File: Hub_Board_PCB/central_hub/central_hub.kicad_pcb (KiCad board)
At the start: 2 copper layers, 0.6 x 1.7 mm, 111 parts, among them J1 CAN_OUT, J2 Conn_01x02, J3 Screw_Terminal_01x08, J4 Screw_Terminal_01x08, J5 CSP-USC16-TR, J6 Screw_Terminal_01x04, J7 Conn_01x03, J8 Conn_01x02, J9 Screw_Terminal_01x04, Q1 BSS138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

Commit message: Central hub layout first draft (+ some changes to motor driver)
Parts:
- removed SW1: SW_Push, Button_Switch_SMD:SW_Push_1P1T_NO_6x6mm_H9.5mm
- removed TP1, TP6: TestPoint, TestPoint:TestPoint_Pad_D1.0mm
- added C20: 10nF, Capacitor_SMD:C_0603_1608Metric, B.Cu at (75.8, 7.70)
- added C21: 10nF, Capacitor_SMD:C_0603_1608Metric, B.Cu at (73.6, 6.40)
- added C22: 10nF, Capacitor_SMD:C_0603_1608Metric, B.Cu at (71.4, 5.00)
- added H1: MountingHole, MountingHole:MountingHole_3mm, F.Cu at (3.00, 3.00)
- added H2: MountingHole, MountingHole:MountingHole_3mm, F.Cu at (105.0, 3.00)
- added H3: MountingHole, MountingHole:MountingHole_3mm, F.Cu at (3.00, 58.7)
- added H4: MountingHole, MountingHole:MountingHole_3mm, F.Cu at (105.0, 58.7)
- C7, C9: moved to B.Cu
- moved J1 283.5 mm to (2.70, 50.3)
- moved R19 269.4 mm to (16.4, 33.6), turned to 0 degrees
- moved R18 265.8 mm to (6.35, 49.0), turned to -90 degrees
- moved D6 264.8 mm to (20.6, 33.6), turned to 180 degrees
- moved R20 263.2 mm to (16.4, 36.7), turned to 0 degrees
- moved D5 262.5 mm to (9.53, 49.0), turned to -90 degrees
- moved D7 258.7 mm to (20.6, 36.7), turned to 180 degrees
- moved U4 248.3 mm to (16.7, 49.0), turned to 90 degrees
- moved Y2 246.9 mm to (37.6, 58.3)
- moved C11 245.8 mm to (33.5, 54.5), turned to 180 degrees
- moved C13 242.7 mm to (36.9, 54.5), turned to 0 degrees
- moved C14 239.3 mm to (21.2, 49.1)
- moved C12 236.9 mm to (27.7, 44.2), turned to 90 degrees
- moved U3 236.9 mm to (33.3, 47.9)
- moved TP9 223.5 mm to (28.7, 40.3)
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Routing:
- net +5V: track 0.00 -> 297.1 mm, vias 0 -> 20
- net +3.3V: track 0.00 -> 169.5 mm, vias 0 -> 11
- net D10: track 0.00 -> 95.9 mm, vias 0 -> 2
- net D13: track 0.00 -> 90.2 mm, vias 0 -> 2
- net D11: track 0.00 -> 80.7 mm, vias 0 -> 2
- net D12: track 0.00 -> 63.1 mm, vias 0 -> 2
- net D5: track 0.00 -> 56.8 mm, vias 0 -> 2
- net GND: track 0.00 -> 56.0 mm, vias 0 -> 48
- net D1: track 0.00 -> 55.7 mm, vias 0 -> 2
- net D0: track 0.00 -> 53.6 mm, vias 0 -> 2
- net D4: track 0.00 -> 51.0 mm, vias 0 -> 2
- net D7: track 0.00 -> 48.5 mm
- net D6: track 0.00 -> 48.4 mm, vias 0 -> 1
- net D2: track 0.00 -> 47.0 mm, vias 0 -> 1
- net D3: track 0.00 -> 45.3 mm, vias 0 -> 1
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- added copper zone on B.Cu, net +12V
- added copper zone on F.Cu, net +12V
- added copper zone on F.Cu, net +5V
- added copper zone on F.Cu, net -BATT
- added copper zone on B.Cu, net GND
- added copper zone on F.Cu, net GND
- added copper zone on F.Cu, net Net-(C25-Pad2)
- added copper zone on F.Cu, net Net-(C27-Pad2)
- added copper zone on F.Cu, net Net-(C30-Pad2)
- added copper zone on F.Cu, net Net-(U7-BST)
- added copper zone on F.Cu, net Net-(U7-SW)
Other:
- board size 0.6 x 1.7 mm -> 108 x 61.7 mm

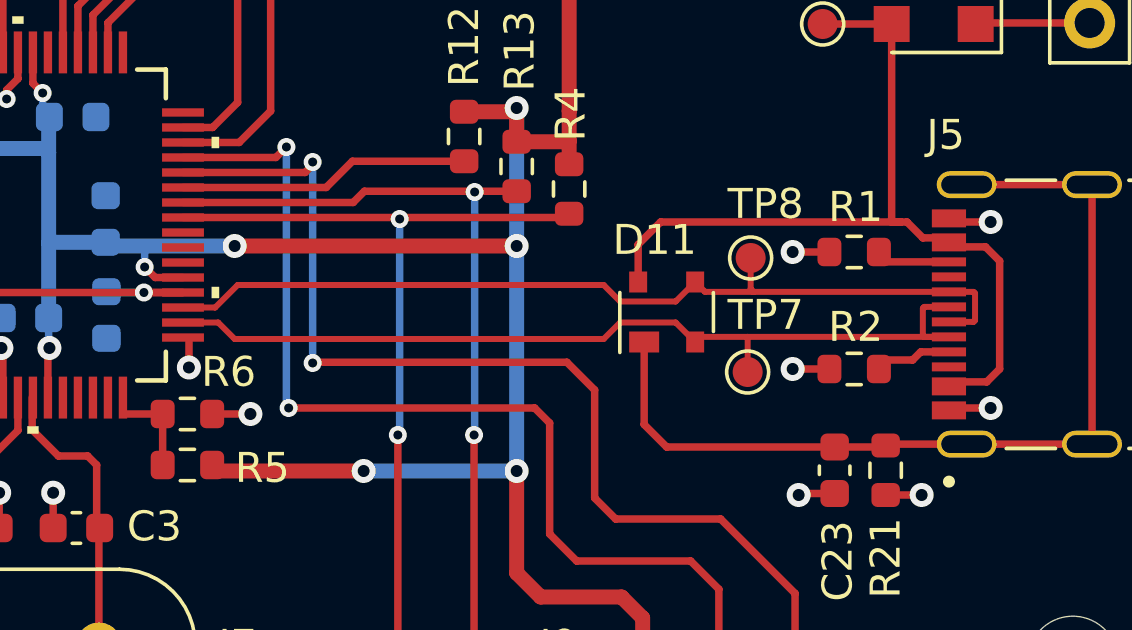
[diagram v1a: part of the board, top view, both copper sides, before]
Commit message: Small changes to USB connector d+ and d- traces
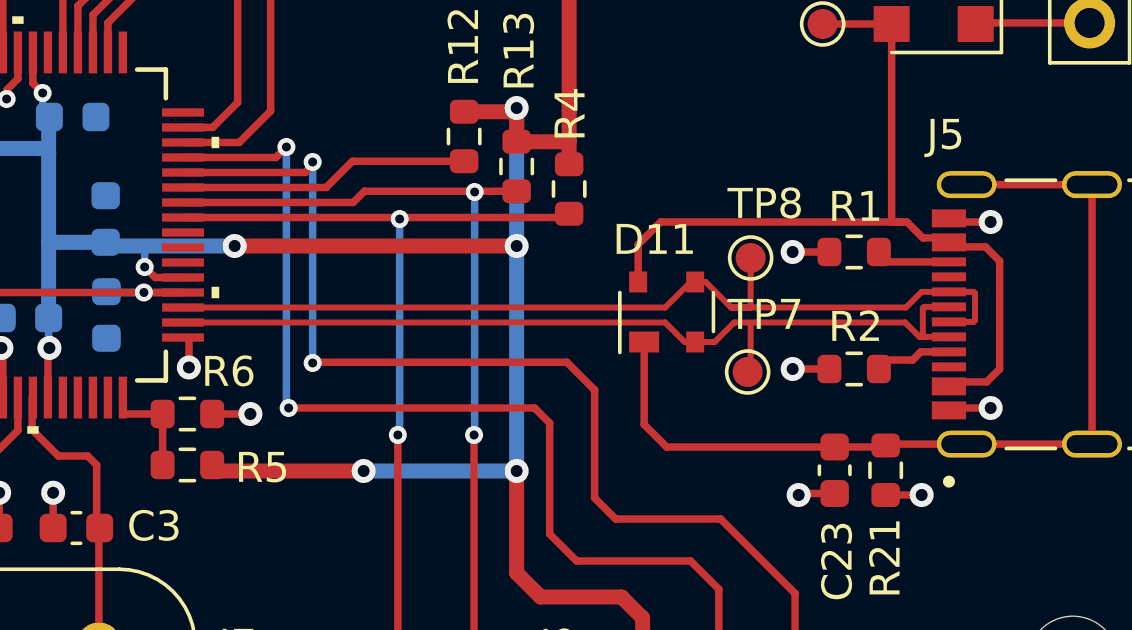
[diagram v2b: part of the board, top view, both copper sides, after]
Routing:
- net USB_D+: track 30.3 -> 31.4 mm
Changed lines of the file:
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@@
   (segment (start 100.04 44.62925) (end 100.91 44.62925) (width 0.25) (layer "F.Cu") (net 25))
   (segment (start 99.51075 44.1) (end 100.04 44.62925) (width 0.25) (layer "F.Cu") (net 25))
-  (segment (start 92.45 48.1) (end 91.8 47.45) (width 0.2) (layer "F.Cu") (net 26))
+  (segment (start 99.45 47.45) (end 99.92925 47.92925) (width 0.2) (layer "F.Cu") (net 26))
   (segment (start 100.09 47.92925) (end 100.91 47.92925) (width 0.2) (layer "F.Cu") (net 26))
-  (segment (start 91.8 47.45) (end 89.95 47.45) (width 0.2) (layer "F.Cu") (net 26))
+  (segment (start 89.95 47.45) (end 89.949181 47.450819) (width 0.2) (layer "F.Cu") (net 26))
+  (segment (start 92.1 48.1) (end 91.45 47.45) (width 0.2) (layer "F.Cu") (net 26))
   (segment (start 100.91 46.92925) (end 100.09 46.92925) (width 0.2) (layer "F.Cu") (net 26))
-  (segment (start 89.4 48) (end 77.1 48) (width 0.2) (layer "F.Cu") (net 26))
-  (segment (start 89.95 47.45) (end 89.4 48) (width 0.2) (layer "F.Cu") (net 26))
-  (segment (start 92.45 48.1) (end 92.62075 47.92925) (width 0.2) (layer "F.Cu") (net 26))
+  (segment (start 99.92925 47.92925) (end 100.09 47.92925) (width 0.2) (layer "F.Cu") (net 26))
+  (segment (start 92.45 48.1) (end 92.1 48.1) (width 0.2) (layer "F.Cu") (net 26))
+  (segment (start 91.45 47.45) (end 89.95 47.45) (width 0.2) (layer "F.Cu") (net 26))
+  (segment (start 93.75 47.45) (end 99.45 47.45) (width 0.2) (layer "F.Cu") (net 26))
   (segment (start 100.04 46.97925) (end 100.04 47.87925) (width 0.2) (layer "F.Cu") (net 26))
-  (segment (start 92.62075 47.92925) (end 94.2 47.92925) (width 0.2) (layer "F.Cu") (net 26))
+  (segment (start 92.45 48.1) (end 93.1 48.1) (width 0.2) (layer "F.Cu") (net 26))
   (segment (start 100.09 46.92925) (end 100.04 46.97925) (width 0.2) (layer "F.Cu") (net 26))
-  (segment (start 77.1 48) (end 76.550819 47.450819) (width 0.2) (layer "F.Cu") (net 26))
-  (segment (start 94.2 47.92925) (end 100.91 47.92925) (width 0.2) (layer "F.Cu") (net 26))
-  (segment (start 94.2 49.1) (end 94.2 47.92925) (width 0.2) (layer "F.Cu") (net 26))
+  (segment (start 93.1 48.1) (end 93.75 47.45) (width 0.2) (layer "F.Cu") (net 26))
   (segment (start 100.04 47.87925) (end 100.09 47.92925) (width 0.2) (layer "F.Cu") (net 26))
-  (segment (start 76.550819 47.450819) (end 75.3781 47.450819) (width 0.2) (layer "F.Cu") (net 26))
+  (segment (start 94.2 49.1) (end 94.3 49) (width 0.2) (layer "F.Cu") (net 26))
+  (segment (start 89.949181 47.450819) (end 75.3781 47.450819) (width 0.2) (layer "F.Cu") (net 26))
+  (segment (start 94.3 49) (end 94.3 47.5) (width 0.2) (layer "F.Cu") (net 26))
   (segment (start 101.73 47.42925) (end 100.91 47.42925) (width 0.2) (layer "F.Cu") (net 27))
-  (segment (start 92.45 46.1) (end 92.77925 46.42925) (width 0.2) (layer "F.Cu") (net 27))
+  (segment (start 99.476782 46.95) (end 99.997532 46.42925) (width 0.2) (layer "F.Cu") (net 27))
+  (segment (start 91.449307 46.950693) (end 75.3781 46.950693) (width 0.2) (layer "F.Cu") (net 27))
+  (segment (start 92.3 46.1) (end 91.449307 46.950693) (width 0.2) (layer "F.Cu") (net 27))
   (segment (start 101.73 46.42925) (end 101.78 46.47925) (width 0.2) (layer "F.Cu") (net 27))
   (segment (start 101.78 47.37925) (end 101.73 47.42925) (width 0.2) (layer "F.Cu") (net 27))
-  (segment (start 91.8 46.75) (end 89.95 46.75) (width 0.2) (layer "F.Cu") (net 27))
-  (segment (start 92.45 46.1) (end 91.8 46.75) (width 0.2) (layer "F.Cu") (net 27))
-  (segment (start 94.3 45.3) (end 94.3 46.32925) (width 0.2) (layer "F.Cu") (net 27))
-  (segment (start 92.77925 46.42925) (end 94.4 46.42925) (width 0.2) (layer "F.Cu") (net 27))
-  (segment (start 76.449307 46.950693) (end 75.3781 46.950693) (width 0.2) (layer "F.Cu") (net 27))
-  (segment (start 94.4 46.42925) (end 100.91 46.42925) (width 0.2) (layer "F.Cu") (net 27))
-  (segment (start 89.4 46.2) (end 77.2 46.2) (width 0.2) (layer "F.Cu") (net 27))
-  (segment (start 94.3 46.32925) (end 94.4 46.42925) (width 0.2) (layer "F.Cu") (net 27))
+  (segment (start 93.65 46.95) (end 99.476782 46.95) (width 0.2) (layer "F.Cu") (net 27))
+  (segment (start 92.45 46.1) (end 92.8 46.1) (width 0.2) (layer "F.Cu") (net 27))
+  (segment (start 93.65 46.95) (end 94.3 46.95) (width 0.2) (layer "F.Cu") (net 27))
+  (segment (start 94.3 46.95) (end 94.3 45.3) (width 0.2) (layer "F.Cu") (net 27))
+  (segment (start 92.8 46.1) (end 93.65 46.95) (width 0.2) (layer "F.Cu") (net 27))
+  (segment (start 99.997532 46.42925) (end 100.91 46.42925) (width 0.2) (layer "F.Cu") (net 27))
   (segment (start 100.91 46.42925) (end 101.73 46.42925) (width 0.2) (layer "F.Cu") (net 27))
-  (segment (start 77.2 46.2) (end 76.449307 46.950693) (width 0.2) (layer "F.Cu") (net 27))
   (segment (start 101.78 46.47925) (end 101.78 47.37925) (width 0.2) (layer "F.Cu") (net 27))
-  (segment (start 89.95 46.75) (end 89.4 46.2) (width 0.2) (layer "F.Cu") (net 27))
+  (segment (start 92.45 46.1) (end 92.3 46.1) (width 0.2) (layer "F.Cu") (net 27))
   (segment (start 3.166833 19.18) (end 2.85 18.863167) (width 0.25) (layer "F.Cu") (net 28))
   (segment (start 3.046833 18.88548) (end 3.046833 15.997313) (width 1) (layer "F.Cu") (net 28))

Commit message: Meeting layout updates
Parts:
- added R35: 0, Resistor_SMD:R_0402_1005Metric, F.Cu at (132.8, 75.6)
- added R36: 0, Resistor_SMD:R_0402_1005Metric, F.Cu at (130.7, 75.6)
- added R37: 0, Resistor_SMD:R_0402_1005Metric, F.Cu at (129.7, 75.6)
- added R7: 0, Resistor_SMD:R_0402_1005Metric, F.Cu at (99.6, 78.7)
- moved G*** 110.6 mm to (80.0, 97.1)
- moved R19 83.0 mm to (89.5, 72.9), turned to -90 degrees
- moved D6 81.5 mm to (89.5, 77.1), turned to 90 degrees
- moved R20 78.8 mm to (86.4, 72.9), turned to -90 degrees
- moved TP9 78.4 mm to (96.7, 79.2)
- moved D7 77.2 mm to (86.4, 77.1), turned to 90 degrees
- moved C11 76.4 mm to (100.8, 90.8)
- moved C13 76.4 mm to (104.2, 90.8)
- moved U3 76.4 mm to (100.5, 84.2)
- moved C12 76.4 mm to (95.0, 80.5)
- moved C14 76.4 mm to (88.5, 85.4)
- moved U4 76.4 mm to (84.0, 85.3)
- moved Y2 76.4 mm to (104.9, 94.6)
- moved TP4 75.3 mm to (107.2, 60.1)
- moved TP5 72.6 mm to (100.0, 61.8)
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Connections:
- U1 pad 34: D11 -> Net-(U1-CTX0/TDO/SWO/GTIOC1A/P109)
- U1 pad 36: D13 -> Net-(U1-GTIOC3A/P111)
- U1 pad 37: D10 -> Net-(U1-GTIOC3B/P112)
- U3 pad 17: D12 -> Net-(U3-SO)
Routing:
- net /MCU/P012: track 18.7 -> 43.9 mm, vias 0 -> 2
- net /MCU/P013: track 19.3 -> 41.5 mm, vias 0 -> 2
- net D11: track 80.7 -> 63.0 mm
- net D10: track 95.9 -> 78.3 mm
- net D12: track 63.1 -> 46.3 mm
- net +5V: track 297.1 -> 284.7 mm
- net +3.3V: track 169.5 -> 157.5 mm
- net D7: track 48.5 -> 38.8 mm
- net D6: track 48.4 -> 39.1 mm
- net D0: track 53.6 -> 44.4 mm
- net D1: track 55.7 -> 46.5 mm
- net /CAN/CAN_HI: track 13.2 -> 22.0 mm
- net /CAN/CAN_LOW: track 13.3 -> 22.0 mm
- net Net-(D6-K): track 30.5 -> 21.9 mm
- net D2: track 47.0 -> 38.5 mm
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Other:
- board text added: "FYDP 2024 Group 26 - Ethan Gilbert - Brandon Phu - Jonathon Ko - Ben Flack"

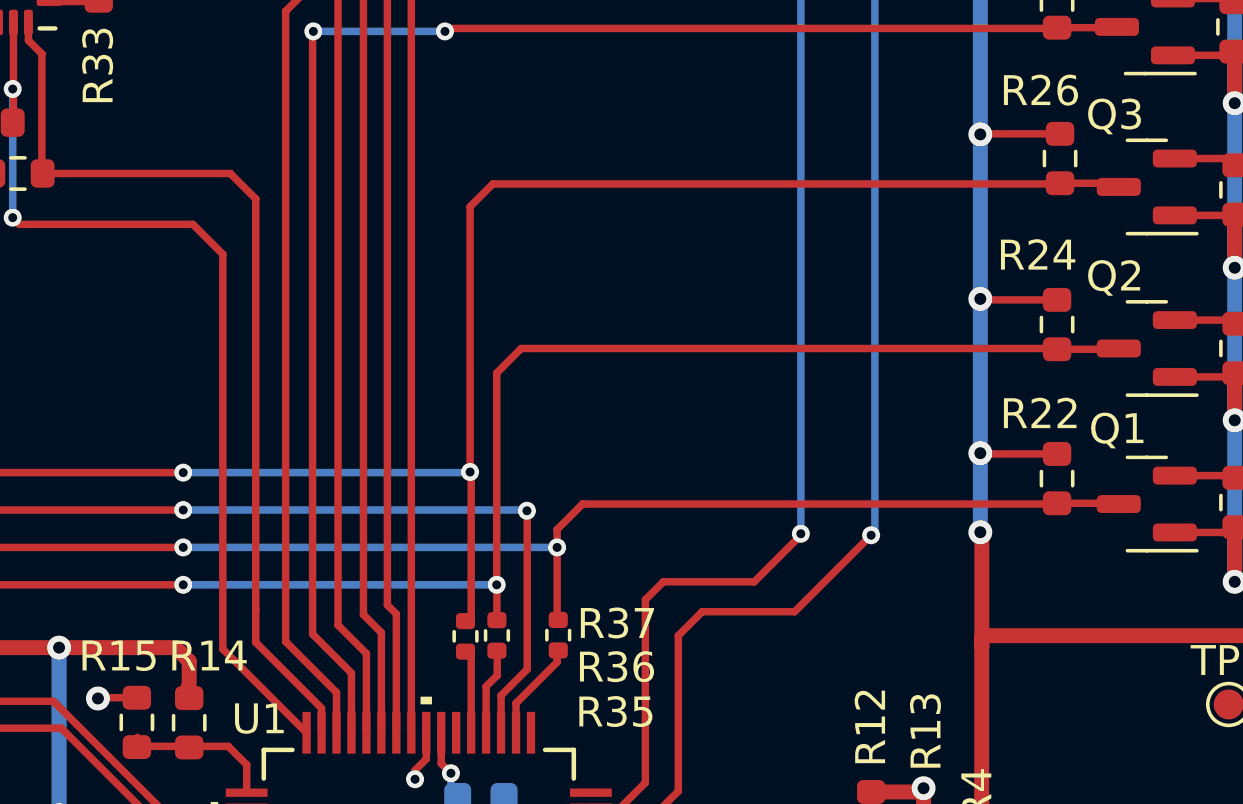
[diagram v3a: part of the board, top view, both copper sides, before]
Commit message: added additional cs pin for display/can
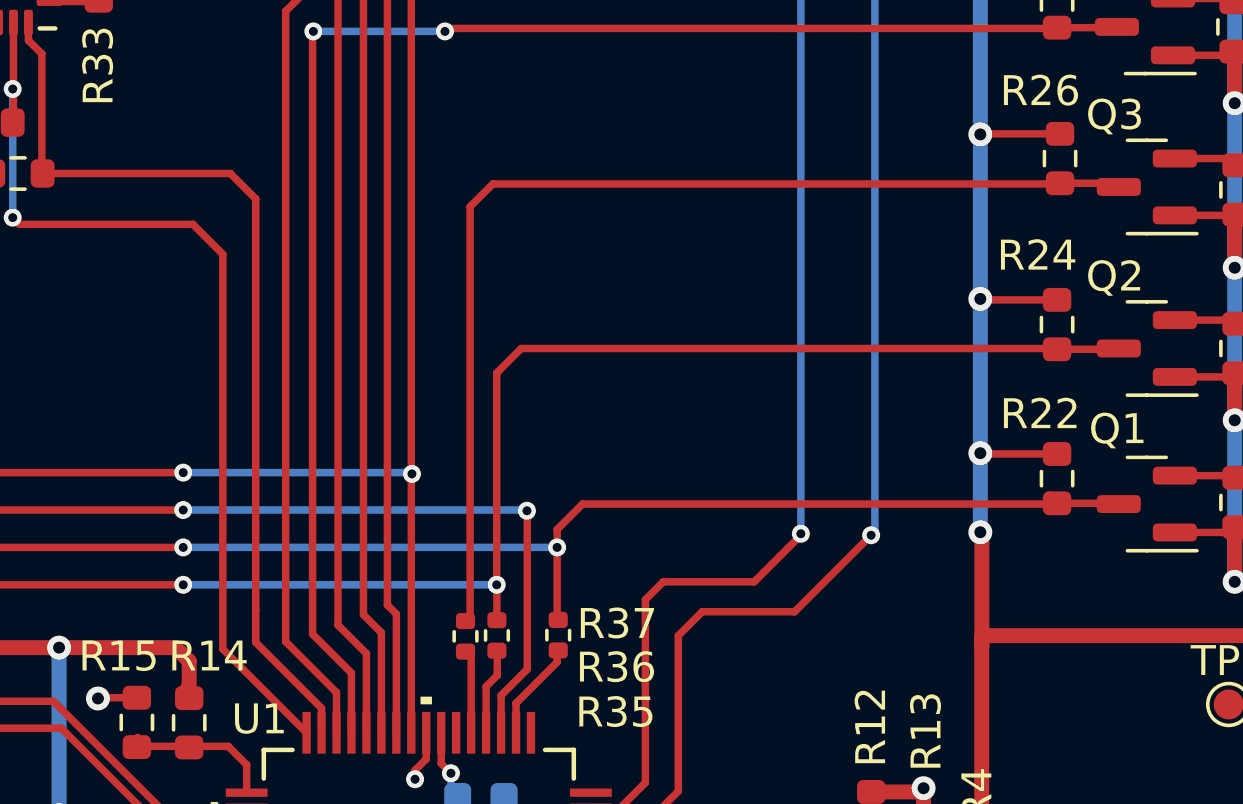
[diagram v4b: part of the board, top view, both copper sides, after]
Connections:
- U3 pad 18: D10 -> D7
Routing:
- net D10: track 78.3 -> 36.0 mm, vias 2 -> 0
- net D7: track 38.8 -> 79.0 mm, vias 0 -> 2
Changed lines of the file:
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@@
       (net 124 "Net-(U3-SO)") (pinfunction "SO") (pintype "output"))
     (pad "18" smd roundrect (at 2.8625 -1.625 90) (size 1.475 0.4) (layers "F.Cu" "F.Paste" "F.Mask") (roundrect_rratio 0.25)
-      (net 31 "D10") (pinfunction "~{CS}") (pintype "input"))
+      (net 32 "D7") (pinfunction "~{CS}") (pintype "input"))
     (pad "19" smd roundrect (at 2.8625 -2.275 90) (size 1.475 0.4) (layers "F.Cu" "F.Paste" "F.Mask") (roundrect_rratio 0.25)
       (net 104 "Net-(U3-~{RESET})") (pinfunction "~{RESET}") (pintype "input"))
@@
   (via (at 132.753167 72.657206) (size 0.6) (drill 0.3) (layers "F.Cu" "B.Cu") (net 30))
   (segment (start 120.253167 72.657206) (end 132.753167 72.657206) (width 0.25) (layer "B.Cu") (net 30))
-  (segment (start 98.925 80.125) (end 98.5 79.7) (width 0.25) (layer "F.Cu") (net 31))
-  (segment (start 130.603167 60.507206) (end 149.540667 60.507206) (width 0.25) (layer "F.Cu") (net 31))
-  (segment (start 129.843044 61.267329) (end 130.603167 60.507206) (width 0.25) (layer "F.Cu") (net 31))
-  (segment (start 98.925 81.3375) (end 98.925 80.125) (width 0.25) (layer "F.Cu") (net 31))
-  (segment (start 98.5 71) (end 99.342794 70.157206) (width 0.25) (layer "F.Cu") (net 31))
-  (segment (start 99.342794 70.157206) (end 120.253167 70.157206) (width 0.25) (layer "F.Cu") (net 31))
+  (segment (start 129.843044 74.966956) (end 129.69 75.12) (width 0.25) (layer "F.Cu") (net 31))
+  (segment (start 129.843044 61.267329) (end 129.843044 74.966956) (width 0.25) (layer "F.Cu") (net 31))
   (segment (start 151.403167 60.482206) (end 151.528167 60.607206) (width 0.25) (layer "F.Cu") (net 31))
-  (segment (start 129.88 74.93) (end 129.69 75.12) (width 0.25) (layer "F.Cu") (net 31))
-  (segment (start 149.540667 60.507206) (end 149.565667 60.482206) (width 0.25) (layer "F.Cu") (net 31))
-  (segment (start 129.843044 70.136591) (end 129.843044 61.267329) (width 0.25) (layer "F.Cu") (net 31))
-  (segment (start 129.843044 70.136591) (end 129.88 70.173547) (width 0.25) (layer "F.Cu") (net 31))
-  (segment (start 129.88 70.173547) (end 129.88 74.93) (width 0.25) (layer "F.Cu") (net 31))
-  (segment (start 98.5 79.7) (end 98.5 71) (width 0.25) (layer "F.Cu") (net 31))
+  (segment (start 149.540667 60.507206) (end 130.603167 60.507206) (width 0.25) (layer "F.Cu") (net 31))
+  (segment (start 130.603167 60.507206) (end 129.843044 61.267329) (width 0.25) (layer "F.Cu") (net 31))
+  (segment (start 149.565667 60.482206) (end 149.540667 60.507206) (width 0.25) (layer "F.Cu") (net 31))
   (segment (start 149.565667 60.482206) (end 151.403167 60.482206) (width 0.25) (layer "F.Cu") (net 31))
-  (via (at 120.253167 70.157206) (size 0.6) (drill 0.3) (layers "F.Cu" "B.Cu") (net 31))
-  (via (at 129.843044 70.136591) (size 0.6) (drill 0.3) (layers "F.Cu" "B.Cu") (net 31))
-  (segment (start 120.253167 70.157206) (end 129.843044 70.157206) (width 0.25) (layer "B.Cu") (net 31))
-  (segment (start 129.843044 70.157206) (end 129.891144 70.109106) (width 0.25) (layer "B.Cu") (net 31))
+  (segment (start 98.925 80.125) (end 98.5 79.7) (width 0.25) (layer "F.Cu") (net 32))
+  (segment (start 98.925 81.3375) (end 98.925 80.125) (width 0.25) (layer "F.Cu") (net 32))
+  (segment (start 98.5 71) (end 99.342794 70.157206) (width 0.25) (layer "F.Cu") (net 32))
+  (segment (start 99.342794 70.157206) (end 120.253167 70.157206) (width 0.25) (layer "F.Cu") (net 32))
   (segment (start 127.878104 49.171896) (end 133.215 43.835) (width 0.25) (layer "F.Cu") (net 32))
   (segment (start 127.878104 78.854106) (end 127.878104 49.171896) (width 0.25) (layer "F.Cu") (net 32))
   (segment (start 133.215 43.835) (end 133.215 42.25) (width 0.25) (layer "F.Cu") (net 32))
+  (segment (start 98.5 79.7) (end 98.5 71) (width 0.25) (layer "F.Cu") (net 32))
+  (via (at 127.9 70.2) (size 0.6) (drill 0.3) (layers "F.Cu" "B.Cu") (net 32))
+  (via (at 120.253167 70.157206) (size 0.6) (drill 0.3) (layers "F.Cu" "B.Cu") (net 32))
+  (segment (start 120.253167 70.157206) (end 127.857206 70.157206) (width 0.25) (layer "B.Cu") (net 32))
   (segment (start 130.675 43.775) (end 130.675 42.25) (width 0.25) (layer "F.Cu") (net 33))
   (segment (start 127.078167 47.371833) (end 130.675 43.775) (width 0.25) (layer "F.Cu") (net 33))

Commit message: Jonathan spelling fix
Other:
- board text added: "FYDP 2024 Group 26 - Ethan Gilbert - Brandon Phu - Jonathan Ko - Ben Flack"
- board text removed: "FYDP 2024 Group 26 - Ethan Gilbert - Brandon Phu - Jonathon Ko - Ben Flack"
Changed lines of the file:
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@@
   (gr_rect (start 58.503167 40.407206) (end 166.543167 102.147206)
     (stroke (width 0.2) (type default)) (fill none) (layer "Edge.Cuts"))
-  (gr_text "FYDP 2024\nGroup 26\n- Ethan Gilbert\n- Brandon Phu\n- Jonathon Ko\n- Ben Flack" (at 83.18 100.14) (layer "B.SilkS")
+  (gr_text "FYDP 2024\nGroup 26\n- Ethan Gilbert\n- Brandon Phu\n- Jonathan Ko\n- Ben Flack" (at 83.18 100.14) (layer "B.SilkS")
     (effects (font (size 1.5 1.5) (thickness 0.3) bold) (justify left bottom mirror))
   )
